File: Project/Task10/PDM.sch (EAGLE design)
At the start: 44 parts

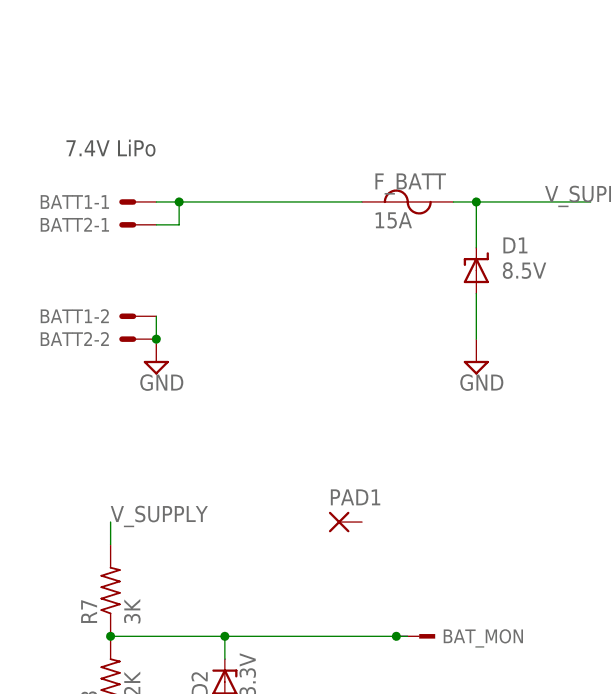
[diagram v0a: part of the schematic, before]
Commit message: Schematic and Board Updated
Schematic is updated with Battery Port XT60 and Caps.
Board is updated with basic placement, not yet routed
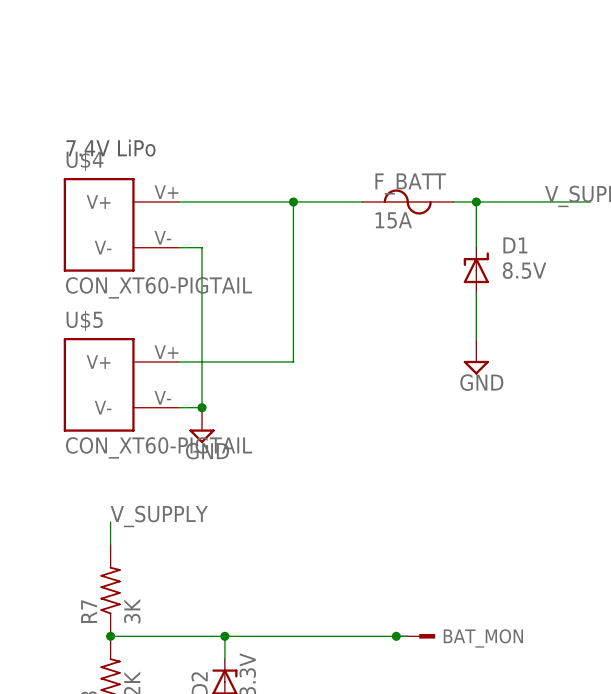
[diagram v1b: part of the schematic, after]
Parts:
- removed BATT1, BATT2: 5566-2, con-molex:5566-2
- removed PAD1: (no value), wirepad:2,15/1,0
- added U$4, U$5: CON_XT60-PIGTAIL, MRSDTeamB:CON_XT60-PIGTAIL
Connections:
- removed net N$10: BATT1-1.S, BATT2-1.S, F_BATT.1
- new net N$2: F_BATT.1, U$4.V+, U$5.V+
- net GND: now also U$4.V-, U$5.V-; no longer BATT1-2.S, BATT2-2.S
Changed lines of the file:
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@@
 <part name="DUE" library="con-molex" deviceset="5566-2" device="" value=""/>
 <part name="SERVO2" library="con-molex" deviceset="5566-2" device="" value=""/>
-<part name="BATT1" library="con-molex" deviceset="5566-2" device="" value=""/>
-<part name="BATT2" library="con-molex" deviceset="5566-2" device="" value=""/>
 <part name="U$1" library="MRSDTeamB" deviceset="MIC29150/29300/29500" device="HORIZONTAL"/>
 <part name="U$2" library="MRSDTeamB" deviceset="MIC29150/29300/29500" device="HORIZONTAL"/>
@@
 <part name="C2" library="rcl" deviceset="CPOL-US" device="TT5D11"/>
 <part name="C4" library="rcl" deviceset="CPOL-US" device="TT5D11"/>
-<part name="PAD1" library="wirepad" deviceset="2,15/1,0" device=""/>
+<part name="U$4" library="MRSDTeamB" deviceset="CON_XT60-" device="PIGTAIL"/>
+<part name="U$5" library="MRSDTeamB" deviceset="CON_XT60-" device="PIGTAIL"/>
 </parts>
 <sheets>
@@
 <instances>
 <instance part="FRAME1" gate="G$1" x="-40.64" y="-10.16"/>
-<instance part="SUPPLY1" gate="GND" x="33.02" y="152.4"/>
+<instance part="SUPPLY1" gate="GND" x="38.1" y="144.78"/>
 <instance part="SUPPLY3" gate="GND" x="256.54" y="167.64"/>
 <instance part="SUPPLY4" gate="GND" x="256.54" y="137.16"/>
@@
 <instance part="SERVO2" gate="-1" x="172.72" y="111.76"/>
 <instance part="SERVO2" gate="-2" x="172.72" y="109.22"/>
-<instance part="BATT1" gate="-1" x="30.48" y="170.18" rot="MR0"/>
-<instance part="BATT1" gate="-2" x="30.48" y="157.48" rot="MR0"/>
-<instance part="BATT2" gate="-1" x="30.48" y="167.64" rot="MR0"/>
-<instance part="BATT2" gate="-2" x="30.48" y="154.94" rot="MR0"/>
 <instance part="U$1" gate="G$1" x="256.54" y="177.8"/>
 <instance part="U$2" gate="G$1" x="256.54" y="147.32"/>
@@
 <instance part="C2" gate="G$1" x="149.86" y="137.16"/>
 <instance part="C4" gate="G$1" x="149.86" y="106.68"/>
-<instance part="PAD1" gate="1" x="53.34" y="134.62"/>
+<instance part="U$4" gate="G$1" x="43.18" y="167.64"/>
+<instance part="U$5" gate="G$1" x="43.18" y="149.86"/>
 </instances>
 <busses>
@@
 </segment>
 </net>
-<net name="N$10" class="0">
-<segment>
-<wire x1="33.02" y1="167.64" x2="35.56" y2="167.64" width="0.1524" layer="91"/>
-<wire x1="33.02" y1="170.18" x2="35.56" y2="170.18" width="0.1524" layer="91"/>
-<wire x1="35.56" y1="170.18" x2="35.56" y2="167.64" width="0.1524" layer="91"/>
-<pinref part="BATT1" gate="-1" pin="S"/>
-<pinref part="BATT2" gate="-1" pin="S"/>
-<pinref part="F_BATT" gate="G$1" pin="1"/>
-<wire x1="35.56" y1="170.18" x2="55.88" y2="170.18" width="0.1524" layer="91"/>
-<junction x="35.56" y="170.18"/>
-</segment>
-</net>
 <net name="GND" class="0">
-<segment>
-<pinref part="SUPPLY1" gate="GND" pin="GND"/>
-<wire x1="33.02" y1="157.48" x2="33.02" y2="154.94" width="0.1524" layer="91"/>
-<pinref part="BATT2" gate="-2" pin="S"/>
-<junction x="33.02" y="154.94"/>
-<pinref part="BATT1" gate="-2" pin="S"/>
-</segment>
 <segment>
 <wire x1="238.76" y1="172.72" x2="238.76" y2="170.18" width="0.1524" layer="91"/>
@@
 <pinref part="SUPPLY7" gate="GND" pin="GND"/>
 <pinref part="ACC1" gate="-2" pin="S"/>
+</segment>
+<segment>
+<pinref part="U$5" gate="G$1" pin="V-"/>
+<pinref part="SUPPLY1" gate="GND" pin="GND"/>
+<wire x1="35.56" y1="147.32" x2="38.1" y2="147.32" width="0.1524" layer="91"/>
+<wire x1="38.1" y1="147.32" x2="38.1" y2="165.1" width="0.1524" layer="91"/>
+<pinref part="U$4" gate="G$1" pin="V-"/>
+<wire x1="38.1" y1="165.1" x2="35.56" y2="165.1" width="0.1524" layer="91"/>
+<junction x="38.1" y="147.32"/>
 </segment>
 </net>
@@
 </segment>
 </net>
+<net name="N$2" class="0">
+<segment>
+<pinref part="U$4" gate="G$1" pin="V+"/>
+<pinref part="F_BATT" gate="G$1" pin="1"/>
+<wire x1="35.56" y1="170.18" x2="48.26" y2="170.18" width="0.1524" layer="91"/>
+<pinref part="U$5" gate="G$1" pin="V+"/>
+<wire x1="48.26" y1="170.18" x2="55.88" y2="170.18" width="0.1524" layer="91"/>
+<wire x1="35.56" y1="152.4" x2="48.26" y2="152.4" width="0.1524" layer="91"/>
+<wire x1="48.26" y1="152.4" x2="48.26" y2="170.18" width="0.1524" layer="91"/>
+<junction x="48.26" y="170.18"/>
+</segment>
+</net>

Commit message: Power Distribution Board Done, minus Power Switch
Mostly board design is done. Just need to add power switch.
The trace width is 423 mil, as calculated by the web
http://circuitcalculator.com/wordpress/?p=25/ , in order to deliver
current of 20A.
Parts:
- U$1, U$2, U$3: value MIC29150/29300/29500HORIZONTAL -> MIC29150/29300/29500VERTICAL; device MRSDTeamB:MIC29150/29300/29500HORIZONTAL -> MRSDTeamB:MIC29150/29300/29500VERTICAL
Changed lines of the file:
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@@
 <part name="DUE" library="con-molex" deviceset="5566-2" device="" value=""/>
 <part name="SERVO2" library="con-molex" deviceset="5566-2" device="" value=""/>
-<part name="U$1" library="MRSDTeamB" deviceset="MIC29150/29300/29500" device="HORIZONTAL"/>
-<part name="U$2" library="MRSDTeamB" deviceset="MIC29150/29300/29500" device="HORIZONTAL"/>
-<part name="U$3" library="MRSDTeamB" deviceset="MIC29150/29300/29500" device="HORIZONTAL"/>
 <part name="F_BATT" library="MRSDTeamB" deviceset="FUSE-" device="ATO" value="15A"/>
 <part name="F_DUE" library="MRSDTeamB" deviceset="FUSE-" device="ATO" value="2A"/>
@@
 <part name="U$4" library="MRSDTeamB" deviceset="CON_XT60-" device="PIGTAIL"/>
 <part name="U$5" library="MRSDTeamB" deviceset="CON_XT60-" device="PIGTAIL"/>
+<part name="U$1" library="MRSDTeamB" deviceset="MIC29150/29300/29500" device="VERTICAL"/>
+<part name="U$2" library="MRSDTeamB" deviceset="MIC29150/29300/29500" device="VERTICAL"/>
+<part name="U$3" library="MRSDTeamB" deviceset="MIC29150/29300/29500" device="VERTICAL"/>
 </parts>
 <sheets>
@@
 All options pin compatible, TO-220-3 Packages </text>
 <text x="236.22" y="187.96" size="1.778" layer="97">Filter capacitors use Kemet 1206 Tantalum</text>
-<text x="22.86" y="175.26" size="1.778" layer="97">7.4V LiPo</text>
+<text x="22.86" y="177.8" size="1.778" layer="97">7.4V LiPo</text>
 </plain>
 <instances>
@@
 <instance part="SERVO2" gate="-1" x="172.72" y="111.76"/>
 <instance part="SERVO2" gate="-2" x="172.72" y="109.22"/>
-<instance part="U$1" gate="G$1" x="256.54" y="177.8"/>
-<instance part="U$2" gate="G$1" x="256.54" y="147.32"/>
-<instance part="U$3" gate="G$1" x="256.54" y="114.3"/>
 <instance part="F_BATT" gate="G$1" x="60.96" y="170.18"/>
 <instance part="F_DUE" gate="G$1" x="142.24" y="172.72"/>
@@
 <instance part="U$4" gate="G$1" x="43.18" y="167.64"/>
 <instance part="U$5" gate="G$1" x="43.18" y="149.86"/>
+<instance part="U$1" gate="G$1" x="256.54" y="177.8"/>
+<instance part="U$2" gate="G$1" x="256.54" y="147.32"/>
+<instance part="U$3" gate="G$1" x="256.54" y="114.3"/>
 </instances>
 <busses>
@@
 <pinref part="C6" gate="G$1" pin="1"/>
 <wire x1="274.32" y1="180.34" x2="271.78" y2="180.34" width="0.1524" layer="91"/>
-<pinref part="U$1" gate="G$1" pin="OUT"/>
 <pinref part="R4" gate="G$1" pin="2"/>
 <wire x1="287.02" y1="180.34" x2="294.64" y2="180.34" width="0.1524" layer="91"/>
@@
 <junction x="287.02" y="180.34"/>
 <pinref part="ACC1" gate="-1" pin="S"/>
+<pinref part="U$1" gate="G$1" pin="OUT"/>
 </segment>
 </net>
@@
 <pinref part="C7" gate="G$1" pin="1"/>
 <wire x1="274.32" y1="149.86" x2="271.78" y2="149.86" width="0.1524" layer="91"/>
-<pinref part="U$2" gate="G$1" pin="OUT"/>
 <wire x1="294.64" y1="149.86" x2="287.02" y2="149.86" width="0.1524" layer="91"/>
 <pinref part="ACC2" gate="-1" pin="S"/>
@@
 <junction x="274.32" y="149.86"/>
 <junction x="287.02" y="149.86"/>
+<pinref part="U$2" gate="G$1" pin="OUT"/>
 </segment>
 </net>
@@
 <pinref part="C10" gate="G$1" pin="1"/>
 <wire x1="274.32" y1="116.84" x2="271.78" y2="116.84" width="0.1524" layer="91"/>
-<pinref part="U$3" gate="G$1" pin="OUT"/>
 <wire x1="294.64" y1="116.84" x2="287.02" y2="116.84" width="0.1524" layer="91"/>
 <pinref part="ACC3" gate="-1" pin="S"/>
@@
 <junction x="274.32" y="116.84"/>
 <junction x="287.02" y="116.84"/>
-</segment>
-</net>
+<pinref part="U$3" gate="G$1" pin="OUT"/>
+</segment>
+</net>

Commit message: More PDM work
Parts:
- removed SERVO1_PWR, SERVO2_PWR: (no value), switch:255SB
- added BATT1, BATT2: CON_XT60-PCB_MOUNT, MRSDTeamB:CON_XT60-PCB_MOUNT
- renumbered C4 to C3, U$4 to BATT1_W, U$5 to BATT2_W
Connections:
- removed net N$12: F_SERVO1.1, SERVO1_PWR.O
- removed net N$14: F_SERVO2.1, SERVO2_PWR.O
- net GND: now also BATT1.V-, BATT2.V-
- net N$11: now also LED3.A; no longer LED4.A
- net N$13: now also LED4.A; no longer LED1.A
- net N$16: now also LED5.A; no longer LED2.A
- net N$2: now also BATT1.V+, BATT2.V+
- net N$22: now also LED6.A; no longer LED3.A
- net N$5: now also LED1.A; no longer LED6.A
- net N$8: now also LED2.A; no longer LED5.A
- net N$9: now also C8.1; no longer C7.1
- net V_SUPPLY: now also C7.1, F_SERVO1.1, F_SERVO2.1; no longer C8.1, SERVO1_PWR.P, SERVO2_PWR.P
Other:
- moved on the sheet: C7, C8, LED1, LED2, LED3, LED4, LED5, LED6

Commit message: Task 10 ready to submit
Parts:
- R7: value 3K -> 15.4K
- R8: value 2.2K -> 10K
- renumbered U$1 to U1, U$2 to U2, U$3 to U3
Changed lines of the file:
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@@
 <part name="R5" library="rcl" deviceset="R-US_" device="R1206" value="1K"/>
 <part name="R6" library="rcl" deviceset="R-US_" device="R1206" value="1K"/>
-<part name="R7" library="rcl" deviceset="R-US_" device="R1206" value="3K"/>
-<part name="R8" library="rcl" deviceset="R-US_" device="R1206" value="2.2K"/>
+<part name="R7" library="rcl" deviceset="R-US_" device="R1206" value="15.4K"/>
+<part name="R8" library="rcl" deviceset="R-US_" device="R1206" value="10K"/>
 <part name="C5" library="rcl" deviceset="C-US" device="C1206K" value="10uF"/>
 <part name="C6" library="rcl" deviceset="C-US" device="C1206K" value="10uF"/>
@@
 <part name="BATT1_W" library="MRSDTeamB" deviceset="CON_XT60-" device="PIGTAIL" value=""/>
 <part name="BATT2_W" library="MRSDTeamB" deviceset="CON_XT60-" device="PIGTAIL" value=""/>
-<part name="U$1" library="MRSDTeamB" deviceset="MIC29150/29300/29500" device="VERTICAL"/>
-<part name="U$2" library="MRSDTeamB" deviceset="MIC29150/29300/29500" device="VERTICAL"/>
-<part name="U$3" library="MRSDTeamB" deviceset="MIC29150/29300/29500" device="VERTICAL"/>
+<part name="U1" library="MRSDTeamB" deviceset="MIC29150/29300/29500" device="VERTICAL" value=""/>
+<part name="U2" library="MRSDTeamB" deviceset="MIC29150/29300/29500" device="VERTICAL" value=""/>
+<part name="U3" library="MRSDTeamB" deviceset="MIC29150/29300/29500" device="VERTICAL" value=""/>
 <part name="BATT2" library="MRSDTeamB" deviceset="CON_XT60-" device="PCB_MOUNT" value=""/>
 <part name="BATT1" library="MRSDTeamB" deviceset="CON_XT60-" device="PCB_MOUNT" value=""/>
@@
 <instance part="BATT1_W" gate="G$1" x="43.18" y="167.64"/>
 <instance part="BATT2_W" gate="G$1" x="43.18" y="149.86"/>
-<instance part="U$1" gate="G$1" x="256.54" y="177.8"/>
-<instance part="U$2" gate="G$1" x="256.54" y="147.32"/>
-<instance part="U$3" gate="G$1" x="256.54" y="114.3"/>
+<instance part="U1" gate="G$1" x="256.54" y="177.8"/>
+<instance part="U2" gate="G$1" x="256.54" y="147.32"/>
+<instance part="U3" gate="G$1" x="256.54" y="114.3"/>
 <instance part="BATT2" gate="G$1" x="43.18" y="187.96"/>
 <instance part="BATT1" gate="G$1" x="43.18" y="205.74"/>
@@
 <junction x="287.02" y="180.34"/>
 <pinref part="ACC1" gate="-1" pin="S"/>
-<pinref part="U$1" gate="G$1" pin="OUT"/>
+<pinref part="U1" gate="G$1" pin="OUT"/>
 </segment>
 </net>
@@
 <junction x="274.32" y="149.86"/>
 <junction x="287.02" y="149.86"/>
-<pinref part="U$2" gate="G$1" pin="OUT"/>
+<pinref part="U2" gate="G$1" pin="OUT"/>
 </segment>
 </net>
@@
 <pinref part="C5" gate="G$1" pin="2"/>
 <pinref part="C6" gate="G$1" pin="2"/>
-<pinref part="U$1" gate="G$1" pin="GND"/>
+<pinref part="U1" gate="G$1" pin="GND"/>
 </segment>
 <segment>
@@
 <pinref part="C7" gate="G$1" pin="2"/>
 <wire x1="238.76" y1="139.7" x2="238.76" y2="142.24" width="0.1524" layer="91"/>
-<pinref part="U$2" gate="G$1" pin="GND"/>
+<pinref part="U2" gate="G$1" pin="GND"/>
 </segment>
 <segment>
@@
 <pinref part="C9" gate="G$1" pin="2"/>
 <wire x1="238.76" y1="106.68" x2="238.76" y2="109.22" width="0.1524" layer="91"/>
-<pinref part="U$3" gate="G$1" pin="GND"/>
+<pinref part="U3" gate="G$1" pin="GND"/>
 </segment>
 <segment>
@@
 <junction x="274.32" y="116.84"/>
 <junction x="287.02" y="116.84"/>
-<pinref part="U$3" gate="G$1" pin="OUT"/>
+<pinref part="U3" gate="G$1" pin="OUT"/>
 </segment>
 </net>
@@
 <wire x1="238.76" y1="180.34" x2="241.3" y2="180.34" width="0.1524" layer="91"/>
 <junction x="238.76" y="180.34"/>
-<pinref part="U$1" gate="G$1" pin="IN"/>
+<pinref part="U1" gate="G$1" pin="IN"/>
 </segment>
 <segment>
@@
 <wire x1="238.76" y1="149.86" x2="241.3" y2="149.86" width="0.1524" layer="91"/>
 <junction x="238.76" y="149.86"/>
-<pinref part="U$2" gate="G$1" pin="IN"/>
+<pinref part="U2" gate="G$1" pin="IN"/>
 </segment>
 <segment>
@@
 <wire x1="238.76" y1="116.84" x2="241.3" y2="116.84" width="0.1524" layer="91"/>
 <junction x="238.76" y="116.84"/>
-<pinref part="U$3" gate="G$1" pin="IN"/>
-</segment>
-<segment>
+<pinref part="U3" gate="G$1" pin="IN"/>
+</segment>
+<segment>
